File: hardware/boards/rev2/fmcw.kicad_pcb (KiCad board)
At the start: 4 copper layers, 119.6 x 141.2 mm, 477 parts, among them CON1 BARREL_JACK, J1 SD_Card, J2 USB_B_Micro, J3 SMA, J4 SMA, J5 SMA, P1 CONN_02X04, P2 CONN_02X04, Q1 DNP(RE1C002UN), Q2 RE1C002UN, SW1 SW_PUSH, U1 LP5907MFX-3.3, U10 LP5907MFX-3.0, U11 LTC2292, U12 ADF4158, U13 TLV172DCK, U14 PAT1220-C-3DB, U15 HMC431LP4, U16 PD4859J5050S2HF, U17 PAT1220-C-5DB, U18 SE5004L, U2 LP5907MFX-1.8, U20 PAT1220-C-6DB, U21 LMV321, U22 TRF37A73, U23 SKY65404, U24 TRF37A73, U25 SKY65404, U26 L7981-fmcw3-rescue, U27 L7981-fmcw3-rescue, U28 L7981-fmcw3-rescue, U29 LP2985A-10DBVR, U3 KT2520K-T, U30 TPS7A91, U31 TPS7A91, U32 TPS7A91, U33 LP5907MFX-3.0, U34 TPS7A91, U35 5400BL15B050E, U36 5400BL15B050E, U37 5400BL15B050E, U38 ADL5802, U39 ADA4940-2, U4 NC7SVU04P5X, U40 TPS7A91, U41 ADA4940-2, U5 NB3N551, U6 XC7A15T-FTG256, U7 W25Q32JV, U8 93LCxxBxxOT, U9 FT2232H, Y1 12MHz

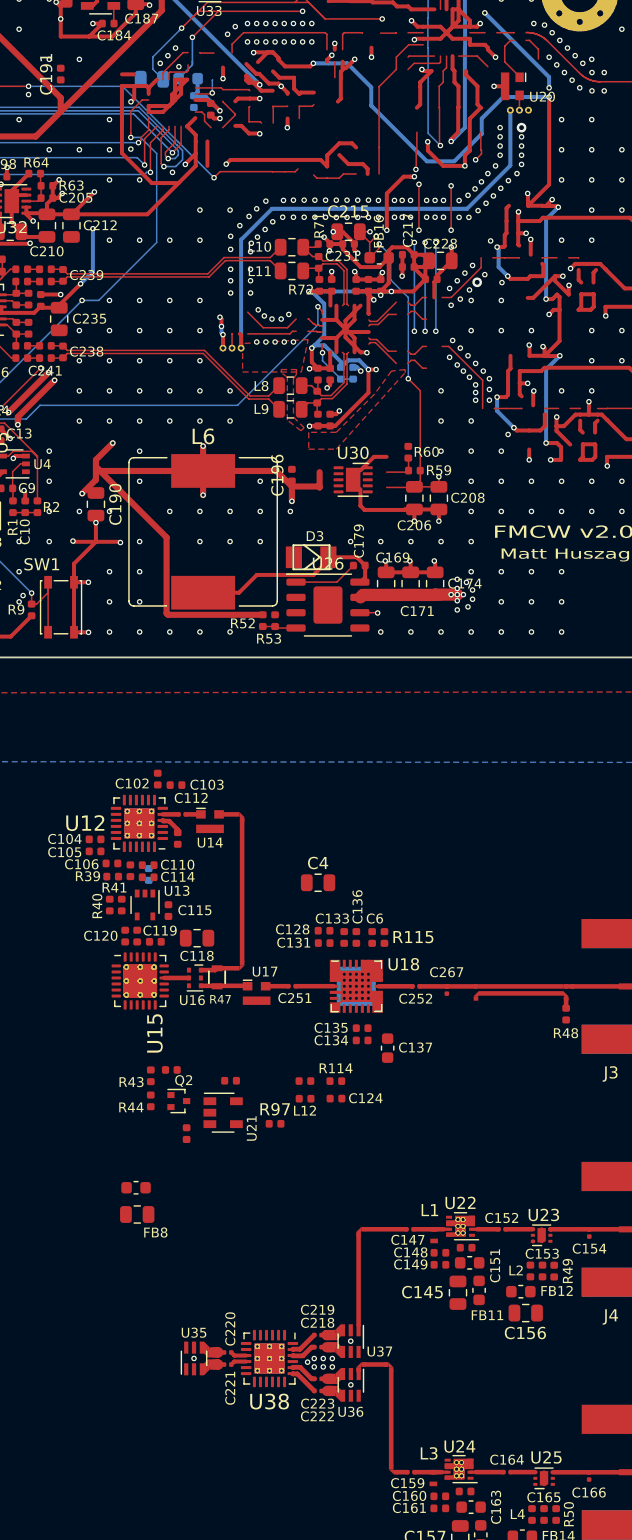
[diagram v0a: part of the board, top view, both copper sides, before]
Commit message: pcb: angle mixer baluns to reduce balanced line length
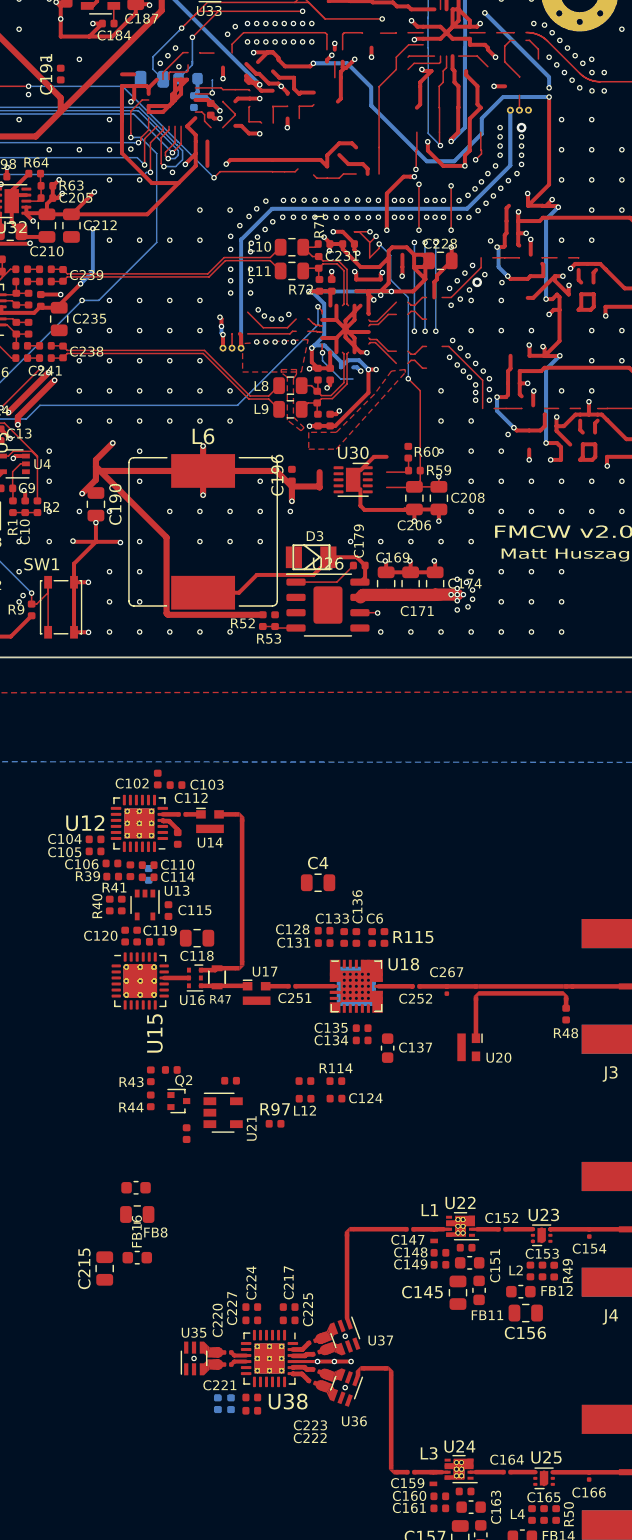
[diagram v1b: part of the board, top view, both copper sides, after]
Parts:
- moved C216 95.8 mm to (171.6, 209.1), turned to 180 degrees
- moved C226 92.8 mm to (171.6, 207.9), turned to 180 degrees
- moved C215 88.3 mm to (159.3, 197.2), turned to 90 degrees
- moved C217 87.9 mm to (174.7, 200.4)
- moved C224 86.6 mm to (171.6, 200.4)
- moved C227 86.3 mm to (171.6, 201.6), turned to 180 degrees
- moved R68 86.2 mm to (168.7, 208.5), turned to 270 degrees
- moved C225 86.2 mm to (174.7, 201.6), turned to 0 degrees
- moved R67 86.0 mm to (169.8, 208.5), turned to 90 degrees
- moved FB16 85.3 mm to (162.1, 196.3)
- moved U20 79.8 mm to (189.6, 178.9)
- moved JP1 0.96 mm to (180.0, 194.0)
- moved C222 0.88 mm to (176.6, 206.7), turned to 340 degrees
- moved C219 0.72 mm to (176.6, 203.3), turned to 20 degrees
- moved C223 0.69 mm to (176.9, 205.7), turned to 340 degrees
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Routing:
- net GND: track 694.1 -> 698.9 mm, vias 635 -> 631
- net Net-(U20-Pad1): track 4.06 -> 7.36 mm
- net /RF1: track 8.42 -> 9.38 mm
- net /mixer/RF2b-: track 5.43 -> 4.62 mm
- net /mixer/RF1b+: track 5.26 -> 4.55 mm
- net Net-(JP1-Pad2): track 7.50 -> 6.90 mm

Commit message: reorganize schematic
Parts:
- removed C128, C133, C134: DNP, Capacitor_SMD:C_0402_1005Metric
- removed C136: 100n, Capacitor_SMD:C_0402_1005Metric
- removed C137: DNP, Capacitor_SMD:C_0603_1608Metric
- removed F1, F2: Via-fmcw3-rescue, fmcw:RF_via
- added H4: MountingHole_Pad, MountingHole:MountingHole_3.2mm_M3_Pad_Via, F.Cu at (83.3, 167.8)
- added JP10: miter_0.38_90deg, fmcw:uwmiter_0.38_0.17_90, F.Cu at (164.4, 216.5)
- added JP9: miter_0.38_90deg, fmcw:uwmiter_0.38_0.17_90, F.Cu at (163.8, 215.9)
- C228, FB8, R98: moved to B.Cu
- U26, U27, U28: value L7981-fmcw3-rescue -> L7980; footprint Package_SO:HSOP-8-1EP_3.9x4.9mm_P1.27mm_EP2.41x3.1mm -> fmcw:HSOP-8-1EP_3.9x4.9mm_P1.27mm_EP2.3x2.3mm_ThermalVias
- moved C259 178.8 mm to (163.3, 238.0)
- moved C255 176.7 mm to (165.3, 238.0)
- moved C254 176.3 mm to (165.4, 235.5)
- moved U41 174.8 mm to (159.4, 234.3), turned to 180 degrees
- moved R98 171.1 mm to (164.3, 236.8)
- moved C258 168.8 mm to (163.4, 235.5)
- moved C243 118.7 mm to (177.1, 231.9)
- moved C242 118.7 mm to (177.1, 230.9)
- moved R76 118.7 mm to (175.1, 231.9)
- moved C239 118.7 mm to (178.6, 231.4)
- moved R75 118.7 mm to (175.1, 230.9)
- moved U39 118.3 mm to (169.6, 234.2)
- moved C240 118.0 mm to (177.1, 236.5)
- moved R73 118.0 mm to (175.1, 236.5)
- moved C241 118.0 mm to (177.1, 237.5)
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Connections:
- net /1V8_OSC renamed Net-(C3-Pad1)
- net /3V3_INV renamed Net-(C5-Pad1)
- net /if/IF1+ renamed /IF1+
- net /if/IF1- renamed /IF1-
- net /if/IF2+ renamed /IF2+
- net /if/IF2- renamed /IF2-
- net Net-(C108-Pad1) renamed /tx/5V_SYNTH
- net Net-(C128-Pad1) renamed /tx/5V_PA
- U18 pad 1: (no net) -> GND
- U18 pad 10: Net-(C137-Pad1) -> (no net)
- U35 pad 1: /LO -> Net-(JP10-Pad2)
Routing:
- net /LO: track 41.6 -> 89.1 mm
- net Net-(C128-Pad1): track 0.00 -> 36.0 mm, vias 0 -> 2
- net /tx/5V_PA: track 36.0 -> 11.1 mm, vias 2 -> 4
- net /if/IF1-: track 0.00 -> 8.81 mm
- net /IF1-: track 8.81 -> 0.00 mm
- net /if/IF2+: track 0.00 -> 8.27 mm
- net /IF2+: track 8.27 -> 0.00 mm
- net Net-(C117-Pad2): track 0.00 -> 8.14 mm
- net GND: track 698.9 -> 707.0 mm, vias 631 -> 638
- net /if/IF2-: track 0.00 -> 7.82 mm
- net /IF2-: track 7.82 -> 0.00 mm
- net /IF1+: track 7.77 -> 0.00 mm
- net /if/IF1+: track 0.00 -> 7.77 mm
- net Net-(C5-Pad1): track 5.44 -> 0.00 mm
- net /3V3_INV: track 0.00 -> 5.44 mm
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- added copper zone on In2.Cu, net /tx/5V_PA
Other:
- board size 119.6 x 141.2 mm -> 125.3 x 83.3 mm
- net class differential_microstrip: clearance 0.005 -> 0.127
- net class gcpw removed
- board text added: "PCB cost (OshPark 4-layer): $10/sq.in. x 3.28in. x 4.93in. = $162"

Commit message: revert to kicad v5 for pcb gen
V6 contains a few bugs and a V6 board cannot be edited with V5.
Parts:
- removed C254, C255, C256, C257, C258, C259, C260, C261, C262, C263: DNP, Capacitor_SMD:C_0402_1005Metric
- removed C264, C265: 100n, Capacitor_SMD:C_0402_1005Metric
- removed C266: DNP, Capacitor_SMD:C_0805_2012Metric
- removed JP1, JP10, JP15, JP16, JP6, JP7, JP8, JP9: miter_0.38_90deg, fmcw:uwmiter_0.38_0.17_90
- removed P1, P2: CONN_02X04, Connector_PinHeader_2.54mm:PinHeader_2x04_P2.54mm_Vertical_SMD
- removed R100, R101, R102, R103, R104, R105, R106, R107, R108, R109, R98, R99: DNP, Resistor_SMD:R_0402_1005Metric
- removed R110, R111, R112, R113: 0, Resistor_SMD:R_0402_1005Metric
- removed U41: ADA4940-2, Package_CSP:LFCSP-24-1EP_4x4mm_P0.5mm_EP2.5x2.5mm
- added C116: 100n, Capacitor_SMD:C_0402_1005Metric, F.Cu at (155.6, -66.6)
- added C12: 100n, Capacitor_SMD:C_0402_1005Metric, F.Cu at (142.9, -50.2)
- added C8: 100n, Capacitor_SMD:C_0402_1005Metric, F.Cu at (138.8, -46.8)
- added FB5: BLM18PG181SH1D, Inductor_SMD:L_0603_1608Metric, F.Cu at (120.2, 6.69)
- added J6: Conn_02x08_Odd_Even, Connector_PinHeader_1.27mm:PinHeader_2x08_P1.27mm_Vertical, F.Cu at (113.2, -9.47)
- added T1: uwave, fmcw_v5:uwm_0.38_0.17_90, F.Cu at (201.9, -59.4)
- added T2: uwave, fmcw_v5:uwm_0.38_0.17_90, F.Cu at (197.5, -55.9)
- added T3: uwave, fmcw_v5:uwm_0.38_0.17_90, F.Cu at (217.9, -13.0)
- added T4: uwave, fmcw_v5:uwm_0.38_0.17_90, F.Cu at (220.3, -16.5)
- added T5: uwave, fmcw_v5:uwm_0.38_0.17_90, F.Cu at (222.3, -16.7)
- added T6: uwave, fmcw_v5:uwm_0.38_0.17_90, F.Cu at (217.9, -11.0)
- added T7: uwave, fmcw_v5:uwm_0.38_0.17_90, F.Cu at (220.3, -14.5)
- added T8: uwave, fmcw_v5:uwm_0.38_0.17_90, F.Cu at (222.1, -14.7)
- C108, C113, C14, C17, C20, C21, C22, C228, C23, C24, C25, C26, C27, C28, C29, C30, C31, C32, C33, C34, C35, C36, C37, C38, C39, C40, C41, C42, C43, C44, C45, C46, C47, C48, C49, C50, C51, C52, C53, C54, C55, C56, C57, C58, C91, C95, FB6, FB8, Q1, R10, R12, R13, R15, R37, R58, R67, R68, R7, R8: moved to F.Cu
- C112, C147, C152, C154, C159, C164, C166, C218, C219, C220, C221, C222, C223, C251, C252, C267: footprint fmcw:RF_C_0201_0603Metric -> fmcw_v5:RF_C_0201_0603Metric
- D3, D4, D5: footprint fmcw:SOD-123F -> Diode_SMD:D_SOD-123F
- J3, J4, J5: footprint fmcw:BU-1420701851_SMA -> fmcw_v5:SMA_901-10512
- JP17, JP2, JP4: footprint fmcw:balun_exit_inv -> fmcw_v5:balun_exit_inv
- JP18, JP3, JP5: footprint fmcw:balun_exit -> fmcw_v5:balun_exit
- L1, L3: footprint fmcw:RF_Bypass_C_0402_1005Metric -> fmcw_v5:RF_Bypass_C_0402_1005Metric
- L10, L11, L8, L9: footprint Inductor_SMD:L_0805_2012Metric -> Inductor_SMD:L_0603_1608Metric
- L5, L6: footprint Inductor_SMD:L_Bourns_SRR1210A -> Inductor_SMD:L_Wuerth_HCI-1365
- L7: footprint fmcw:SRR6040A -> fmcw_v5:SRR6040A
- R47: footprint fmcw:R_0603b -> fmcw_v5:R_0603b
- U15: value HMC431LP4 -> HMC431
- U18: footprint fmcw:Skyworks_SE5004L -> fmcw_v5:Skyworks_SE5004L
- U22, U24: footprint fmcw:WSON-8-1EP_2x2mm_P0.5mm_EP0.9x1.6mm_ThermalVias -> fmcw_v5:WSON-8-1EP_2x2mm_P0.5mm_EP0.9x1.6mm_ThermalVias
- U26, U27, U28: footprint fmcw:HSOP-8-1EP_3.9x4.9mm_P1.27mm_EP2.3x2.3mm_ThermalVias -> fmcw_v5:HSOP-8-1EP_3.9x4.9mm_P1.27mm_EP2.3x2.3mm_ThermalVias
- U6: footprint fmcw:FTG256 -> Package_BGA:Xilinx_FTG256
- Y1: footprint fmcw:ABM10 -> Crystal:Crystal_SMD_Abracon_ABM10-4Pin_2.5x2.0mm
- Z1: footprint fmcw:coupler_20db -> fmcw_v5:coupler_20db
- moved C168 302.6 mm to (231.9, -69.1)
- moved C157 301.1 mm to (227.5, -69.1), turned to 0 degrees
- moved L4 300.6 mm to (239.6, -69.6), turned to 0 degrees
- moved C163 300.0 mm to (236.2, -69.3), turned to 0 degrees
- moved FB14 298.1 mm to (231.6, -66.4), turned to 0 degrees
- moved C166 297.2 mm to (242.3, -69.7), turned to 0 degrees
- moved C159 296.1 mm to (237.7, -67.2), turned to 0 degrees
- moved C162 295.9 mm to (235.0, -66.6), turned to 0 degrees
- moved FB13 294.4 mm to (227.3, -62.8), turned to 0 degrees
- moved C165 294.3 mm to (234.4, -64.1), turned to 0 degrees
- moved U24 292.3 mm to (227.5, -65.8), turned to 0 degrees
- moved C161 290.8 mm to (229.7, -60.6)
- moved U25 290.4 mm to (231.3, -63.6), turned to 0 degrees
- moved C160 289.4 mm to (226.8, -60.6)
- moved R50 285.7 mm to (226.8, -56.6), turned to 0 degrees
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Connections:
- net /fpga/usb/USBDM renamed /fpga/usb/USBDa_N
- net /fpga/usb/USBDP renamed /fpga/usb/USBDa_P
- net Net-(C246-Pad2) renamed /if/IF2c+
- net Net-(C248-Pad1) renamed /if/IF2c-
- net Net-(C249-Pad1) renamed /if/IF1c-
- net Net-(R20-Pad1) renamed /fpga/usb/USBD_N
- net Net-(R21-Pad1) renamed /fpga/usb/USBD_P
- C236 pad 1: /IF2- -> /if/IF2-
- C236 pad 2: /IF2+ -> /if/IF2+
- C237 pad 1: /IF1- -> /if/IF1-
- C237 pad 2: /IF1+ -> /if/IF1+
- C247 pad 1: Net-(C247-Pad1) -> /if/IF1c+
- C59 pad 1: /3V3D -> /fpga/usb/3V3_IO
- C65 pad 2: /3V3D -> /fpga/usb/3V3_IO
- C71 pad 1: /3V3D -> /fpga/usb/3V3_IO
- C72 pad 1: /3V3D -> /fpga/usb/3V3_IO
- C73 pad 1: /3V3D -> /fpga/usb/3V3_IO
- C74 pad 1: /3V3D -> /fpga/usb/3V3_IO
- L10 pad 1: /IF1- -> /if/IF1-
- L11 pad 1: /IF1+ -> /if/IF1+
- L8 pad 1: /IF2- -> /if/IF2-
- L9 pad 1: /IF2+ -> /if/IF2+
- R17 pad 1: /3V3D -> /fpga/usb/3V3_IO
- R22 pad 2: /3V3D -> /fpga/usb/3V3_IO
- R3 pad 1: /3V3D -> /fpga/usb/3V3_IO
- R4 pad 1: /ADF_REF -> /FPGA_REF
- R47 pad 2: Net-(JP7-Pad1) -> Net-(R47-Pad2)
- R5 pad 1: /FPGA_REF -> /ADC_REF
- R69 pad 1: /IF2- -> /if/IF2-
- R70 pad 2: /IF2+ -> /if/IF2+
- R71 pad 1: /IF1- -> /if/IF1-
- R72 pad 2: /IF1+ -> /if/IF1+
- R76 pad 1: Net-(C247-Pad2) -> /if/IF1c+
- R80 pad 1: Net-(C247-Pad1) -> Net-(C247-Pad2)
- R80 pad 2: Net-(C247-Pad2) -> /if/IF1c+
- R81 pad 1: /ADC_REF -> /ADF_REF
- R82 pad 1: /3V3D -> /fpga/usb/3V3_IO
- U14 pad 2: Net-(JP6-Pad2) -> Net-(R47-Pad2)
- U15 pad 1: (no net) -> GND
- U15 pad 10: (no net) -> GND
- U15 pad 11: (no net) -> GND
- U15 pad 12: (no net) -> GND
- U15 pad 13: (no net) -> GND
- U15 pad 14: (no net) -> GND
- U15 pad 17: (no net) -> GND
- U15 pad 18: (no net) -> GND
- U15 pad 19: (no net) -> GND
- U15 pad 2: (no net) -> GND
- U15 pad 21: (no net) -> GND
- U15 pad 23: (no net) -> GND
- U15 pad 24: (no net) -> GND
- U15 pad 3: (no net) -> GND
- U15 pad 4: (no net) -> GND
- U15 pad 5: (no net) -> GND
- U15 pad 6: (no net) -> GND
- U15 pad 7: (no net) -> GND
- U15 pad 8: (no net) -> GND
- U15 pad 9: (no net) -> GND
- U16 pad 6: Net-(JP7-Pad1) -> Net-(R47-Pad2)
- U20 pad 1: Net-(U20-Pad1) -> /LO
- U20 pad 2: /LO -> Net-(U20-Pad2)
- U35 pad 1: Net-(JP10-Pad2) -> /LO
- U36 pad 1: Net-(JP16-Pad2) -> /RF2
- U37 pad 1: Net-(JP1-Pad2) -> /RF1
- U38 pad 15: /IF2- -> /if/IF2-
- U38 pad 16: /IF2+ -> /if/IF2+
- U38 pad 3: /IF1- -> /if/IF1-
- U38 pad 4: /IF1+ -> /if/IF1+
- U39 pad 12: Net-(C256-Pad2) -> /ADC1-
- U39 pad 13: Net-(C257-Pad2) -> /ADC1+
- U39 pad 18: Net-(C254-Pad2) -> /ADC2+
- U39 pad 19: Net-(C255-Pad2) -> /ADC2-
- U39 pad 5: Net-(C247-Pad1) -> Net-(C247-Pad2)
- U39 pad 6: Net-(C247-Pad2) -> /if/IF1c+
- U8 pad 6: /3V3D -> /fpga/usb/3V3_IO
- U9 pad 20: /3V3D -> /fpga/usb/3V3_IO
- U9 pad 31: /3V3D -> /fpga/usb/3V3_IO
- U9 pad 42: /3V3D -> /fpga/usb/3V3_IO
- U9 pad 50: /3V3D -> /fpga/usb/3V3_IO
- U9 pad 56: /3V3D -> /fpga/usb/3V3_IO
- Z1 pad 3: Net-(U20-Pad1) -> Net-(U20-Pad2)
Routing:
- net GND: track 707.0 -> 243.5 mm, vias 638 -> 353
- net /3V3D: track 333.3 -> 28.9 mm, vias 47 -> 16
- net /power/12V: track 209.1 -> 0.00 mm, vias 33 -> 0
- net /3V6: track 181.0 -> 0.00 mm, vias 12 -> 0
- net /3V0: track 94.2 -> 0.00 mm, vias 17 -> 0
- net /3V3A: track 101.4 -> 17.2 mm, vias 14 -> 10
- net /MIX_ENBL: track 78.4 -> 0.00 mm, vias 2 -> 0
- net /fpga/PROGRAM_B: track 72.0 -> 0.00 mm, vias 2 -> 0
- net /1V0: track 76.4 -> 4.58 mm, vias 5 -> 3
- net /1V8: track 79.2 -> 9.39 mm, vias 6 -> 4
- net /5VPA: track 66.3 -> 0.00 mm, vias 6 -> 0
- net /5V: track 63.0 -> 0.00 mm, vias 15 -> 0
- net /ADF_DATA: track 62.1 -> 0.00 mm, vias 2 -> 0
- net /fpga/TDO: track 61.0 -> 0.00 mm, vias 4 -> 0
- net /PA_OFF: track 59.6 -> 0.00 mm, vias 2 -> 0
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- added copper zone on In2.Cu, net /fpga/usb/3V3_IO
- removed copper zone on In2.Cu, net /10V
- removed copper zone on In2.Cu, net /1V0
- removed copper zone on In2.Cu, net /1V8
- removed copper zone on In2.Cu, net /3V0
- removed copper zone on In2.Cu, net /3V3A
- removed copper zone on In2.Cu, net /3V3D
- removed copper zone on In2.Cu, net /3V6
- removed copper zone on In2.Cu, net /5V
- removed copper zone on In2.Cu, net /fpga/adc/3V0
- removed copper zone on In2.Cu, net /fpga/usb/1V8
- removed copper zone on In2.Cu, net /mixer/5VF
- removed copper zone on In2.Cu, net /power/12V
- removed copper zone on In2.Cu, net /power/5V6
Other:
- board size 125.3 x 83.3 mm -> 94.6 x 83.4 mm
- net class 1.5A removed
- net class 1000mA added: clearance 0.127, trace_width 1.5, via_dia 0.4572, via_drill 0.254
- net class 1500mA added: clearance 0.127, trace_width 2.7, via_dia 0.4572, via_drill 0.254
- net class 300mA added: clearance 0.127, trace_width 0.3, via_dia 0.4572, via_drill 0.254
- net class 3A removed
- net class 500mA added: clearance 0.127, trace_width 0.6, via_dia 0.4572, via_drill 0.254
- net class Power removed
- board text added: "PCB cost (OshPark 4-layer): $10/sq.in. x 3.28in. x 3.72in. = $122"
- board text removed: "PCB cost (OshPark 4-layer): $10/sq.in. x 3.28in. x 4.93in. = $162"
